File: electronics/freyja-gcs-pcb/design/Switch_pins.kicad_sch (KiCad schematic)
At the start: 85 parts, among them J10 XT60PB-M.G.Y, J11 XT60PB-F.G.Y, Q10 NPN, Q11 NPN, Q12 NPN, Q13 NPN, Q14 NPN, Q15 NPN, Q16 NPN, Q17 NPN, Q18 NPN, Q19 NPN, Q20 NPN, Q21 NPN, Q22 NPN, Q23 NPN, Q26 NPN, Q9 NPN, SW10 PB22E09071, SW11 ST-0-102-A01-T000-LF+PJ, SW12 ST-0-102-A01-T000-LF+PJ, SW13 ST-0-102-A01-T000-LF+PJ, SW14 ST-0-102-A01-T000-LF+PJ, SW4 PB22E09071, SW5 ST-0-102-A01-T000-LF+PJ, SW6 ST-0-102-A01-T000-LF+PJ, SW7 PB22E09071, SW8 ST-0-102-A01-T000-LF+PJ, SW9 ST-0-102-A01-T000-LF+PJ

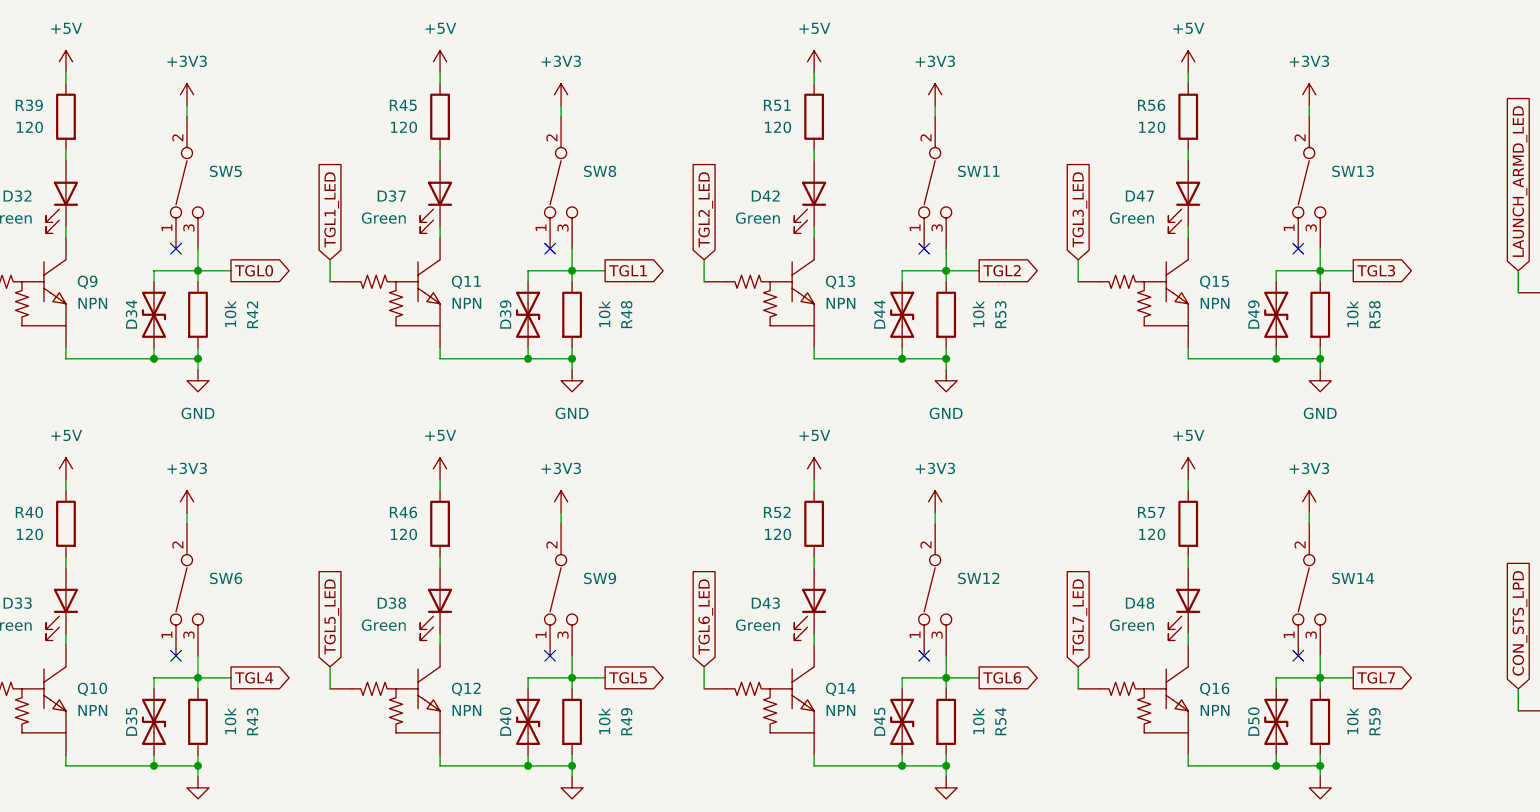
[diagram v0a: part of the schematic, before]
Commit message: change to available parts
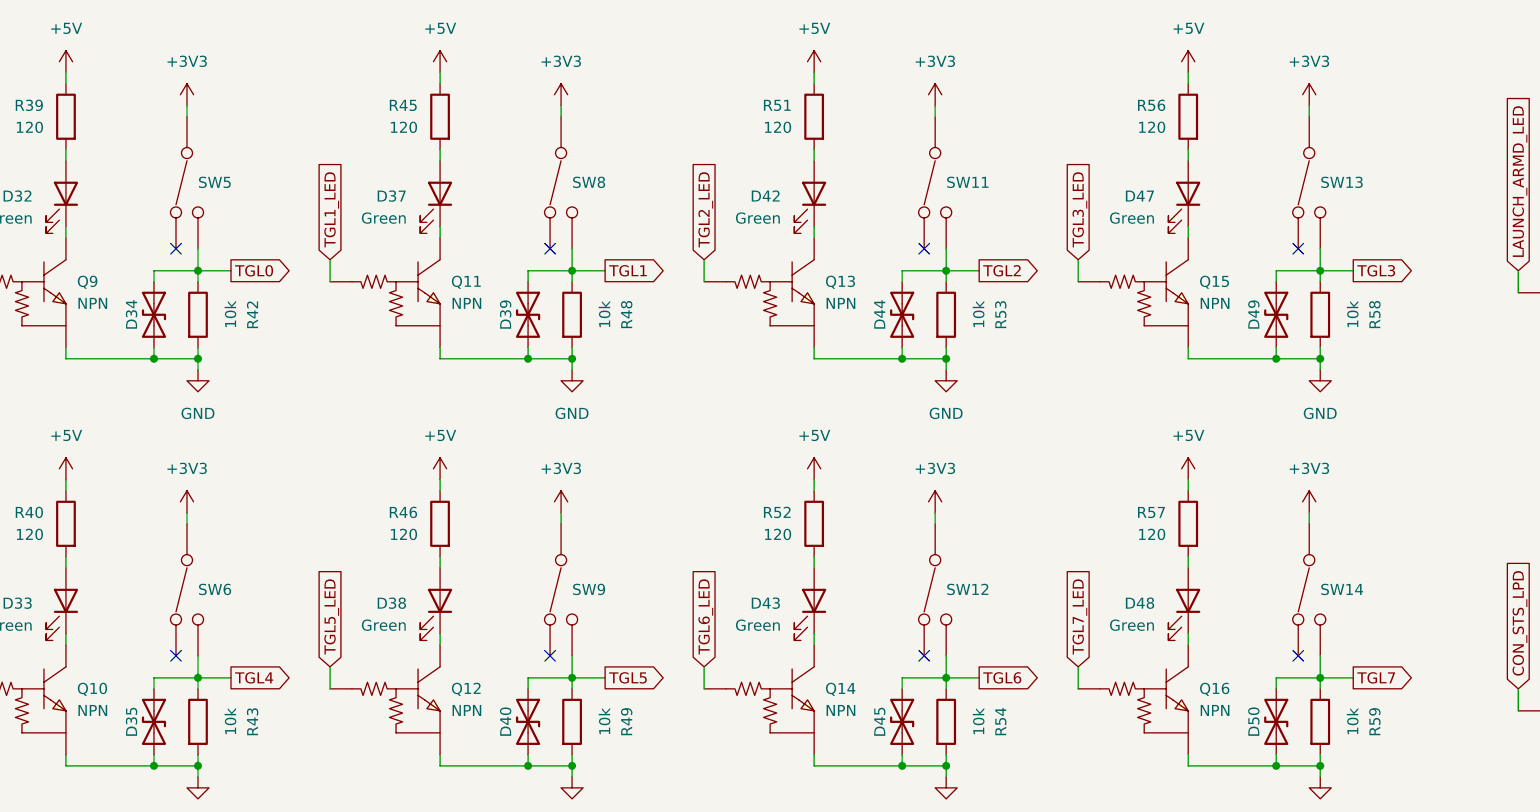
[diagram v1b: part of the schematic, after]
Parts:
- R39, R40, R45, R46, R51, R52, R56, R57, R61, R63, R66: LCSC Part C23186 -> C22787
- SW11, SW12, SW13, SW14, SW5, SW6, SW8, SW9: value ST-0-102-A01-T000-LF+PJ -> 2MS1T1B1M2QES; footprint EasyEDA:SW-TH_3P-L8.3-W5.2-P2.54_ST-0-102-A01-T000 -> EasyEDA:SW-TH_2MS1T1B1M2QES-5; symbol EasyEDA:ST-0-102-A01-T000-LF+PJ -> EasyEDA:2MS1T1B1M2QES-5; LCSC Part C1788487 -> C908280
